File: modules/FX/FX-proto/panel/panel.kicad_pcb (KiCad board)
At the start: 2 copper layers, 40.3 x 128.5 mm, 12 parts

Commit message: FX module - prototype wip
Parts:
- added REF**: MountingHole_PCB_3.2mm_M3, -lmp-holes:MountingHole_PCB_3.2mm_M3, F.Cu at (80.2, 62.4)
- moved REF** 18.7 mm to (70.8, 66.4)
- moved REF** 18.7 mm to (89.5, 65.4)
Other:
- board text added: "AMOUNT"
- board text added: "IN"
- board text added: "MIX"
- board text added: "MODE"
- board text added: "OUT"
- board text added: "TEMPO"
- board text added: "TIME"
- board text added: "TONE"
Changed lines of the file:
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@@
   )
   (footprint "-lmp-holes:MountingHole_Pot_SongHuei" (layer "F.Cu")
-    (at 89.5 66.39)
+    (at 70.8 66.39)
     (descr "Mounting Hole for Alpha RD901F potentiometer")
     (tags "mounting hole Alpha RD901F potentiometer")
@@
     (pad "" np_thru_hole circle locked (at 0 0) (size 3.2 3.2) (drill 3.2) (layers *.Cu *.Mask))
   )
+  (footprint "-lmp-holes:MountingHole_PCB_3.2mm_M3" (layer "F.Cu")
+    (at 80.15 62.36)
+    (descr "Mounting Hole 3.2mm, no annular, M3")
+    (tags "mounting hole 3.2mm m3")
+    (clearance 1.15)
+    (attr exclude_from_pos_files exclude_from_bom)
+    (fp_text reference "REF**" (at 0 0) (layer "F.SilkS") hide
+      (effects (font (size 1 1) (thickness 0.15)))
+    )
+    (fp_text value "MountingHole_PCB_3.2mm_M3" (at 0 0.009) (layer "F.Fab")
+      (effects (font (size 1 1) (thickness 0.15)))
+    )
+    (fp_text user "${REFERENCE}" (at 0.3 0) (layer "F.Fab")
+      (effects (font (size 1 1) (thickness 0.15)))
+    )
+    (fp_circle (center 0 0) (end 2.7686 0) (layer "B.CrtYd") (width 0.0508) (fill none))
+    (fp_circle (center 0 0) (end 2.7686 0) (layer "F.CrtYd") (width 0.0508) (fill none))
+    (pad "" np_thru_hole circle (at 0 0) (size 3.2 3.2) (drill 3.2) (layers *.Cu *.Mask))
+  )
   (footprint "-lmp-holes:MountingHole_Pot_SongHuei" (layer "F.Cu")
     (at 70.8 82.98)
@@
   )
   (footprint "-lmp-holes:MountingHole_SW_Push_C&K_D6R" locked (layer "F.Cu")
-    (at 70.8 65.36)
+    (at 89.5 65.36)
     (descr "Mounting Hole for Alpha RD901F potentiometer")
     (tags "mounting hole Alpha RD901F potentiometer")
@@
     (effects (font (size 1 1) (thickness 0.15)) (justify left mirror))
   )
+  (gr_text "TONE" (at 70.739 108.157) (layer "F.SilkS")
+    (effects (font (size 2.54 2.54) (thickness 0.381)))
+  )
+  (gr_text "TEMPO" (at 89.5 73.787) (layer "F.SilkS")
+    (effects (font (size 2.54 2.54) (thickness 0.381)))
+  )
+  (gr_text "IN" (at 81.25 169.397) (layer "F.SilkS")
+    (effects (font (size 2.54 2.54) (thickness 0.381)))
+  )
+  (gr_text "AMOUNT" (at 89.5 108.157) (layer "F.SilkS")
+    (effects (font (size 2.54 2.54) (thickness 0.381)))
+  )
+  (gr_text "TIME" (at 89.5 90.377) (layer "F.SilkS")
+    (effects (font (size 2.54 2.54) (thickness 0.381)))
+  )
+  (gr_text "MIX" (at 70.739 90.377) (layer "F.SilkS")
+    (effects (font (size 2.54 2.54) (thickness 0.381)))
+  )
+  (gr_text "MODE" (at 70.8 73.787) (layer "F.SilkS")
+    (effects (font (size 2.54 2.54) (thickness 0.381)))
+  )
+  (gr_text "OUT" (at 94.6 169.397) (layer "F.SilkS")
+    (effects (font (size 2.54 2.54) (thickness 0.381)))
+  )
   (zone (net 0) (net_name "") (layers F&B.Cu) (hatch edge 0.508)

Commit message: FX module - prototype gerbers
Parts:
- G1, G3: moved to F.Cu
- moved G1 11.6 mm to (73.3, 128.8), turned to 0 degrees
- moved G3 9.60 mm to (81.5, 128.5), turned to 0 degrees
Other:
- board text added: "FX-proto"
- board text removed: "FX"

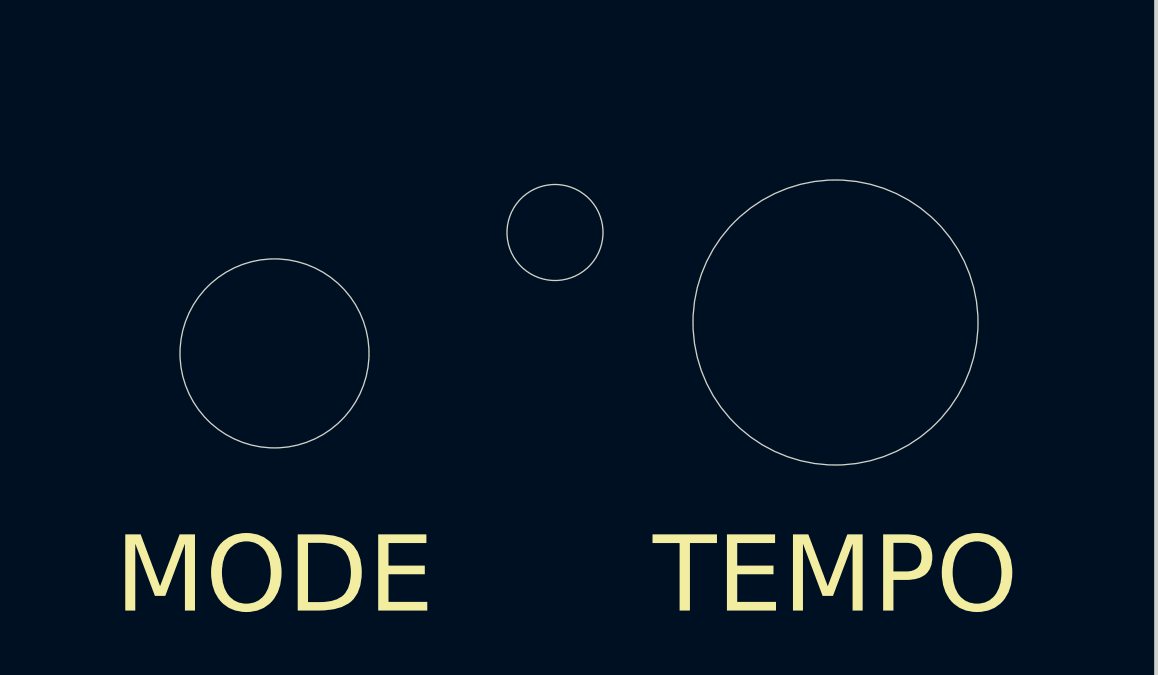
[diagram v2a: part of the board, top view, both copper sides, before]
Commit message: FX module - prototype - adjust hole positions
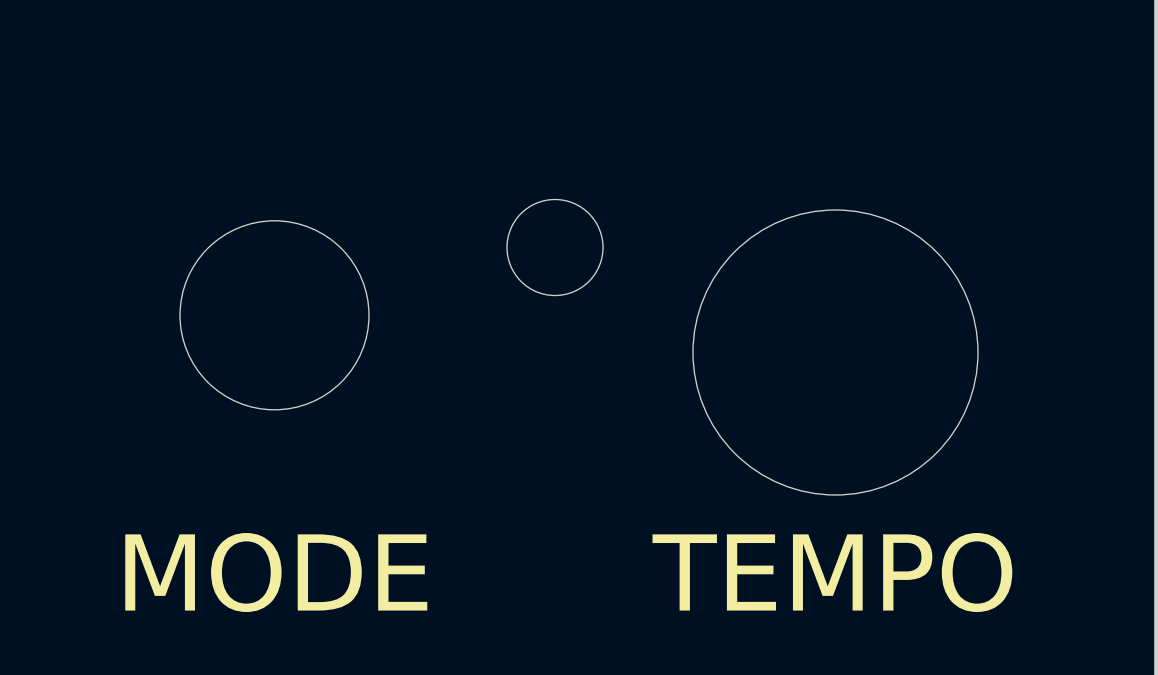
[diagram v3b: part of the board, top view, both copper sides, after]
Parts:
- moved REF** 1.27 mm to (70.8, 65.1)
- moved REF** 1.00 mm to (89.5, 66.4)
- moved REF** 0.50 mm to (80.2, 62.9)
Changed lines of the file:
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@@
   )
   (footprint "-lmp-holes:MountingHole_Pot_SongHuei" (layer "F.Cu")
-    (at 70.8 66.39)
+    (at 70.8 65.12)
     (descr "Mounting Hole for Alpha RD901F potentiometer")
     (tags "mounting hole Alpha RD901F potentiometer")
@@
   )
   (footprint "-lmp-holes:MountingHole_PCB_3.2mm_M3" (layer "F.Cu")
-    (at 80.15 62.36)
+    (at 80.15 62.86)
     (descr "Mounting Hole 3.2mm, no annular, M3")
     (tags "mounting hole 3.2mm m3")
@@
   )
   (footprint "-lmp-holes:MountingHole_SW_Push_C&K_D6R" locked (layer "F.Cu")
-    (at 89.5 65.36)
+    (at 89.5 66.36)
     (descr "Mounting Hole for Alpha RD901F potentiometer")
     (tags "mounting hole Alpha RD901F potentiometer")
